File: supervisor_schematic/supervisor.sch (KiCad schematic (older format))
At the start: 25 parts

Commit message: more supervisor schem work
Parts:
- added C?: CP1, symbol Device:CP1
- added D?: LED, symbol Device:LED
- added J?: Conn_02x03_Odd_Even, symbol Connector_Generic:Conn_02x03_Odd_Even
- added Jack: PJ-059A, PJ059A, symbol Noggin:PJ-059A
- added R9: 330, symbol Device:R
- gave numbers to parts that had none: 2
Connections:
- net labels added: IO0, RX, TX
- wire segments 55 -> 68
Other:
- note added: "Enable"
- moved on the sheet: 10K, ANT?, C2, C3, D1, D2, LS?, R1, R2, R3, R4, R5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

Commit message: supervisor almost done
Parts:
- removed C1: 1u, symbol pspice:C
- removed J?: Conn_02x03_Odd_Even, symbol Connector_Generic:Conn_02x03_Odd_Even
- removed U?: OLED-1602A, symbol Noggin:OLED-1602A
- added C1: 1u, symbol Device:CP1
- added IC?: PCF8574DW, SOIC127P1030X265-16N, symbol Noggin:PCF8574DW
- added J1: Conn_01x06_Female, symbol Connector:Conn_01x06_Female
- added U?: OLED-1602A, symbol Noggin:OLED-1602A
- gave numbers to parts that had none: 1
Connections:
- net labels added: RESET
- wire segments 68 -> 80
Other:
- note added: "Button Debouncing"
- note added: "Buzzer"
- note added: "LED Screen\n"
- note added: "Power via a Jack"
- note added: "Programming Header"
- note added: "Will be using a usbC to serial module that will connect via these connectors. \nhttps://www.superhouse.tv/product/espflasher-esp8266-esp32-usb-serial-flasher/"
- note removed: "Enable"
- moved on the sheet: 10K, ANT?, C2, C3, D1, D2, LS1, R1, R2, R3, R4, R5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

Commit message: schem v1 done
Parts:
- added U?: RFM9-LoRa-Radio, symbol Noggin2:RFM9-LoRa-Radio
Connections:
- net +3V3: now also U?.1 (VIN)
- net CLK: now also U?.5 (SCK)
- net CS: now also U?.8 (CS)
- net GND: now also U?.2 (GND)
- net SD0: now also IC?.15 (SDA)
- net SD1: now also IC?.14 (SCL)
- net SD2: now reaches ANT?.17 (SD2)
- net SD2: now also U?.6 (MISO)
- net SD3: now reaches ANT?.18 (SD3)
- net SD3: now also U?.7 (MOSI)
- net IO16: now reaches ANT?.27 (IO16)
- net IO16: now also U?.3 (EN)
- net IO17: now reaches ANT?.28 (IO17)
- net IO18: now reaches ANT?.30 (IO18)
- net IO18: now also U?.9 (RST)
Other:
- note added: "LoRa for wireless communication"
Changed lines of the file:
@@
 	1    0    0    -1
 $EndComp
-Text GLabel 9200 2200 2    50   Input ~ 0
+Text GLabel 9200 2250 2    50   Input ~ 0
 SD1
-Text GLabel 9200 2100 2    50   Input ~ 0
+Text GLabel 9200 2150 2    50   Input ~ 0
 SD0
 $Comp
@@
 Wire Notes Line
 	8550 1000 8550 1650
+$Comp
+L Noggin2:RFM9-LoRa-Radio U?
+U 1 1 621CB351
+P 5700 6700
+F 0 "U?" V 4875 6650 50  0000 C CNN
+F 1 "RFM9-LoRa-Radio" V 4966 6650 50  0000 C CNN
+F 2 "" H 5700 6700 50  0001 C CNN
+F 3 "" H 5700 6700 50  0001 C CNN
+	1    5700 6700
+	0    1    1    0
+$EndComp
+$Comp
+L power:+3.3V #PWR?
+U 1 1 621CE098
+P 5350 6100
+F 0 "#PWR?" H 5350 5950 50  0001 C CNN
+F 1 "+3.3V" H 5365 6273 50  0000 C CNN
+F 2 "" H 5350 6100 50  0001 C CNN
+F 3 "" H 5350 6100 50  0001 C CNN
+	1    5350 6100
+	1    0    0    -1
+$EndComp
+$Comp
+L power:GND #PWR?
+U 1 1 621CEF67
+P 5350 6250
+F 0 "#PWR?" H 5350 6000 50  0001 C CNN
+F 1 "GND" V 5355 6122 50  0000 R CNN
+F 2 "" H 5350 6250 50  0001 C CNN
+F 3 "" H 5350 6250 50  0001 C CNN
+	1    5350 6250
+	0    1    1    0
+$EndComp
+Text GLabel 4250 3200 2    50   Input ~ 0
+IO16
+Text GLabel 5350 6400 0    50   Input ~ 0
+IO16
+Text GLabel 4250 3300 2    50   Input ~ 0
+IO17
+Text GLabel 5300 6550 0    50   Input ~ 0
+IO17
+Text GLabel 5350 6700 0    50   Input ~ 0
+CLK
+Text GLabel 2850 4200 0    50   Input ~ 0
+SD2
+Text GLabel 2850 4300 0    50   Input ~ 0
+SD3
+Text GLabel 5350 6850 0    50   Input ~ 0
+SD2
+Text GLabel 5350 7000 0    50   Input ~ 0
+SD3
+Text GLabel 5350 7150 0    50   Input ~ 0
+CS
+Text GLabel 5350 7300 0    50   Input ~ 0
+IO18
+Text GLabel 4250 3500 2    50   Input ~ 0
+IO18
+Wire Notes Line
+	4850 5650 6350 5650
+Wire Notes Line
+	6350 5650 6350 7600
+Wire Notes Line
+	6350 7600 4850 7600
+Wire Notes Line
+	4850 7600 4850 5650
+Text Notes 5000 5750 0    50   ~ 0
+LoRa for wireless communication
 $EndSCHEMATC

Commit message: going to layout supervisor
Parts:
- removed C?: CP1, symbol Device:CP1
- removed IC?: PCF8574DW, SOIC127P1030X265-16N, symbol Noggin:PCF8574DW
- added CP4: 10u, Capacitor_SMD:C_0805_2012Metric_Pad1.15x1.40mm_HandSolder, symbol Device:CP1
- added CP5: 0.1u, Capacitor_SMD:C_0805_2012Metric_Pad1.15x1.40mm_HandSolder, symbol Device:CP1
- added IC1: PCF8574DW, Connector_PinHeader_2.54mm:PinHeader_1x04_P2.54mm_Vertical, symbol Noggin:PCF8574DW
- added VR1: U1V10F5, Connector_PinHeader_2.54mm:PinHeader_1x03_P2.54mm_Vertical, symbol Noggin2:U1V10F5
- ANT1: renamed from ANT?; footprint ESP32WROOM32D -> Noggin:ESP32WROOM32D
- C1, C2, C3, D1, D2: footprint (none) -> Capacitor_SMD:C_0805_2012Metric_Pad1.15x1.40mm_HandSolder
- D3: renamed from D?; footprint (none) -> Capacitor_SMD:C_0805_2012Metric_Pad1.15x1.40mm_HandSolder
- J1: footprint (none) -> Connector_PinHeader_2.54mm:PinHeader_1x06_P2.54mm_Vertical
- Jack1: renamed from Jack; footprint PJ059A -> Noggin:PJ059A
- LS1: footprint PS1240P02BT -> Noggin:PS1240P02BT
- R1, R2, R3, R4, R5, R7, R8, R9: footprint (none) -> Resistor_SMD:R_0805_2012Metric_Pad1.15x1.40mm_HandSolder
- R6: renamed from 10K; value R6 -> 10K; footprint (none) -> Resistor_SMD:R_0805_2012Metric_Pad1.15x1.40mm_HandSolder
- SW1, SW2, SW3: renamed from SW?; footprint (none) -> Button_Switch_THT:SW_PUSH_6mm
- U1: renamed from U?; footprint (none) -> Package_DIP:DIP-14_W7.62mm
- U2: renamed from U?; footprint (none) -> Noggin:RFM9x
- gave numbers to parts that had none: 1
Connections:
- net +3V3: now also CP4.1, CP5.1, VR1.3 (VIN); no longer U3.~ (VSS)
- net GND: now also CP4.2, CP5.2, IC1.1 (A0), IC1.2 (A1), IC1.3 (A2), IC1.8 (GND), VR1.2 (GND)
- net SDA: now reaches ANT1.33 (IO21)
- net SDA: now also IC1.15 (SDA)
- net SCL: now reaches ANT1.36 (IO22)
- net SCL: now also IC1.14 (SCL)
- new net: IC1.10 (P5), U3.~ (VSS)
- new net: IC1.11 (P6), U3.~ (VSS)
- new net: IC1.4 (P0), U3.~ (VSS)
- new net: IC1.5 (P1), U3.~ (VSS)
- new net: IC1.6 (P2), U3.~ (VSS)
- new net: IC1.7 (P3), U3.~ (VSS)
- new net: IC1.9 (P4), U3.~ (VSS)
- new net +5V: IC1.16 (VCC), U3.~ (VSS), VR1.1 (VOUT)
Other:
- note added: "3V to 5V"
- note added: "LED Screen\nusing module\n"
- note removed: "LED Screen\n"

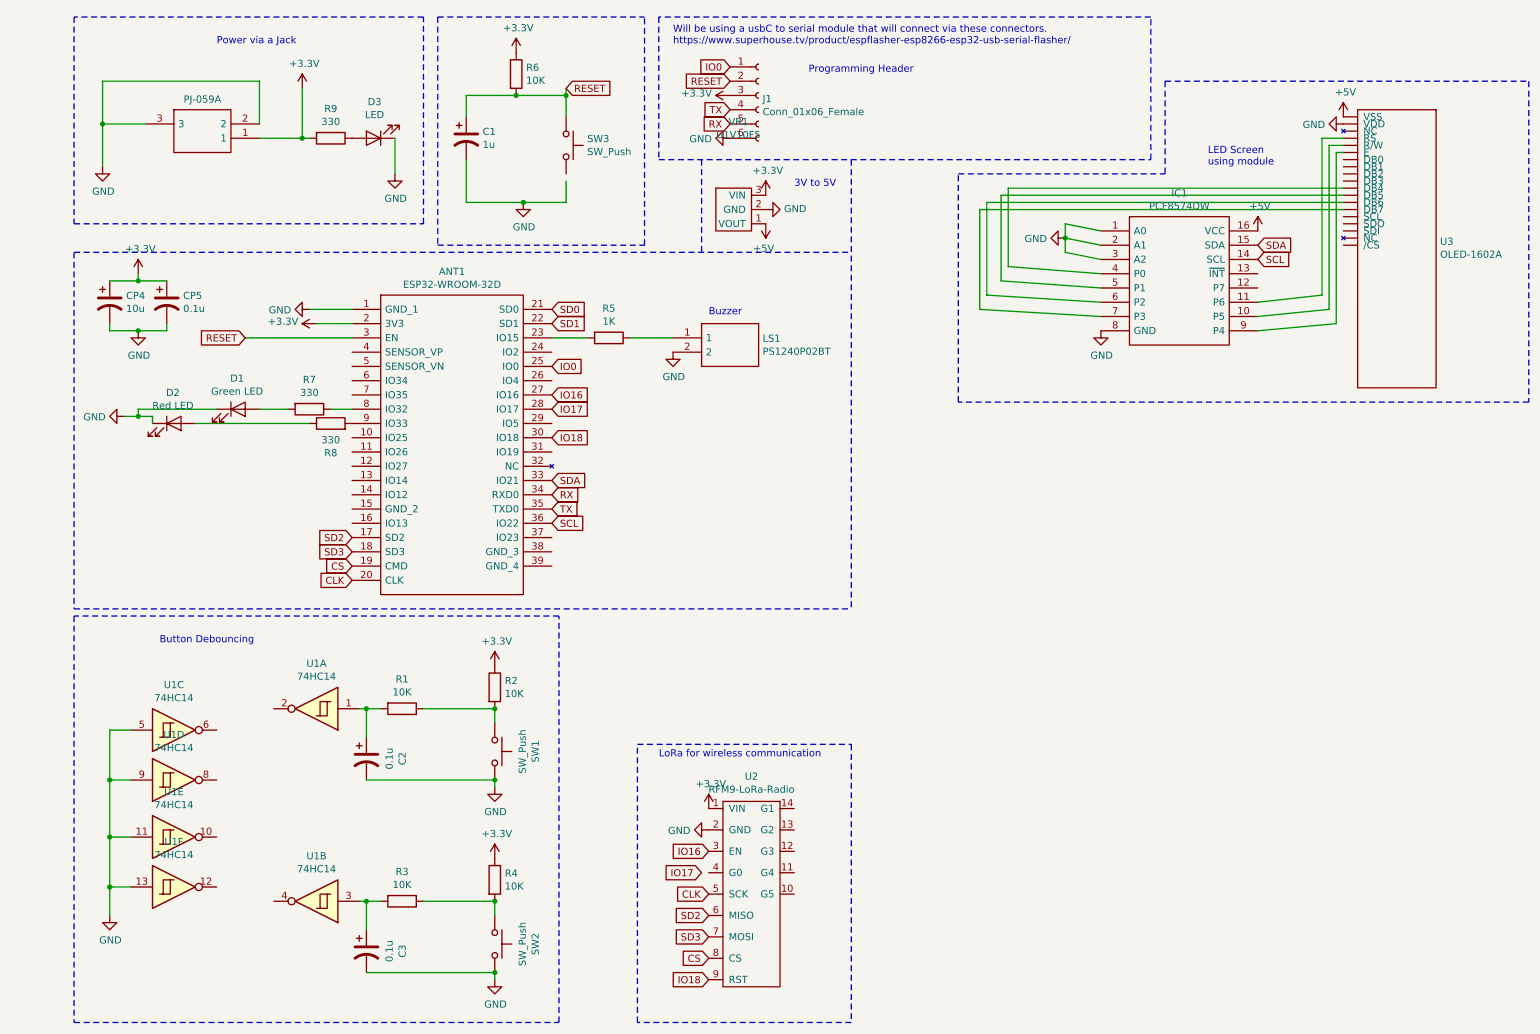
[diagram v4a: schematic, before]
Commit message: ratsnest supervisor
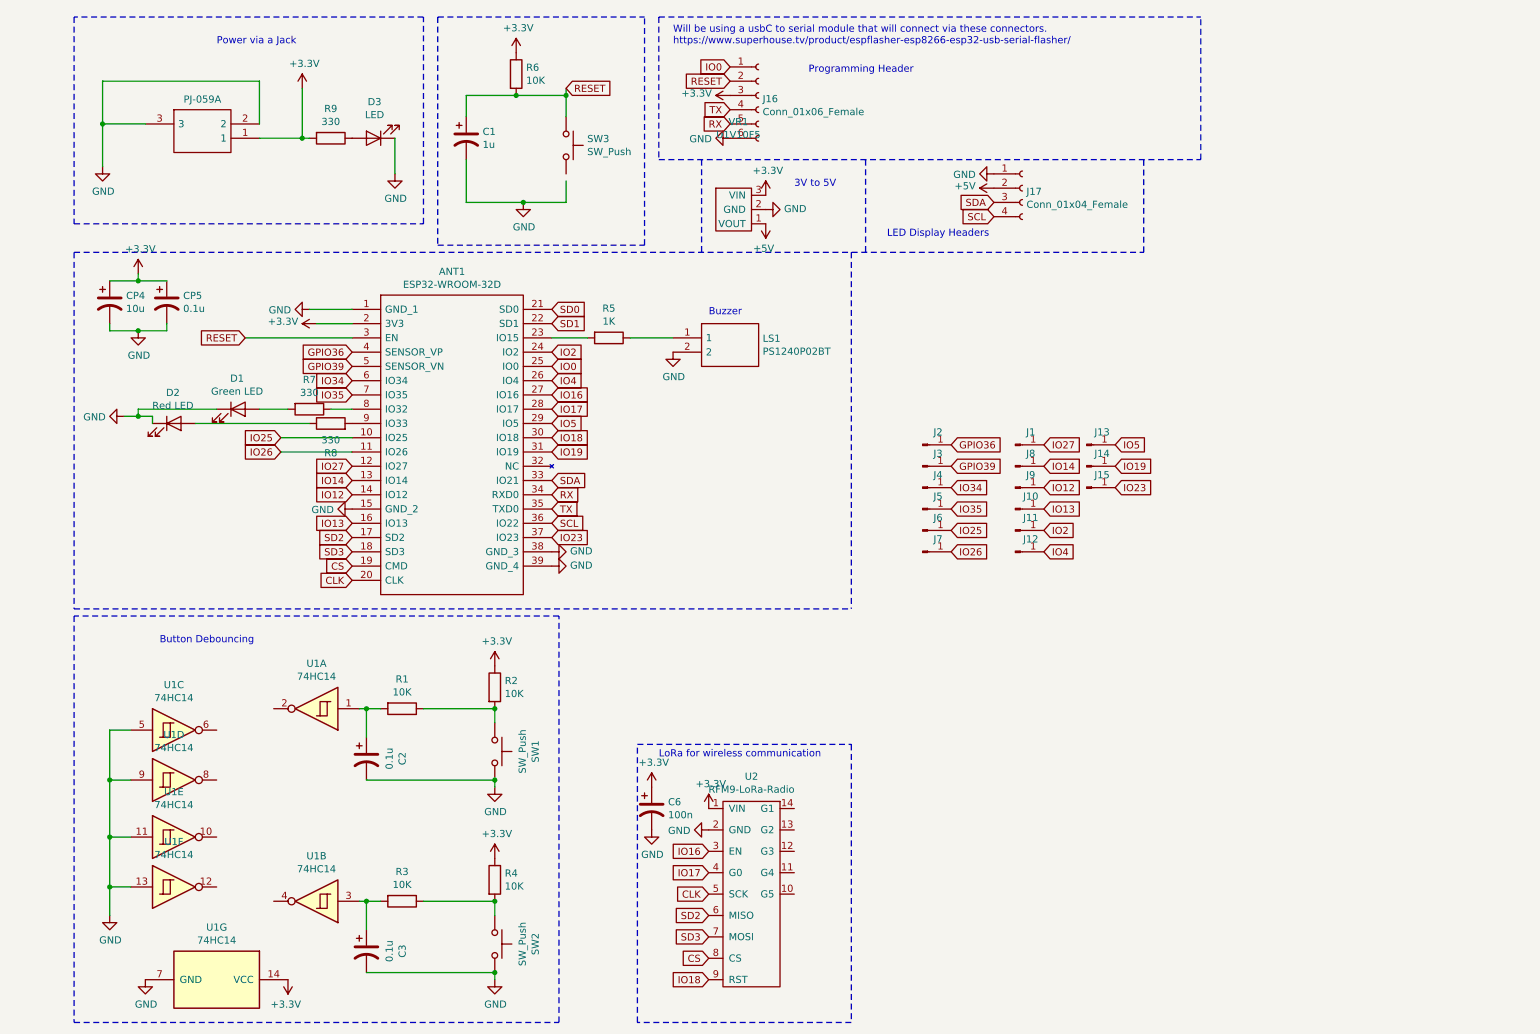
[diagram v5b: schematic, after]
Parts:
- removed IC1: PCF8574DW, Connector_PinHeader_2.54mm:PinHeader_1x04_P2.54mm_Vertical, symbol Noggin:PCF8574DW
- removed U3: OLED-1602A, symbol Noggin:OLED-1602A
- added C6: 100n, Capacitor_SMD:C_0805_2012Metric_Pad1.15x1.40mm_HandSolder, symbol Device:CP1
- added J1, J10, J11, J12, J13, J14, J15, J2, J3, J4, J5, J6, J7, J8, J9: J, Connector_PinHeader_2.54mm:PinHeader_1x01_P2.54mm_Vertical, symbol Connector:Conn_01x01_Male
- added J17: Conn_01x04_Female, symbol Connector:Conn_01x04_Female
- added unit 7 of U1
- VR1: footprint Connector_PinHeader_2.54mm:PinHeader_1x03_P2.54mm_Vertical -> Noggin:U1V10F5-VR
- renumbered J1 to J16
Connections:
- net +3V3: now also C6.1, U1.14 (VCC)
- net +5V: now also J17.2 (Pin_2)
- net GND: now also ANT1.15 (GND_2), ANT1.38 (GND_3), ANT1.39 (GND_4), C6.2, J17.1 (Pin_1), U1.7 (GND)
- net IO17: now also U2.4 (G0)
- net SCL: now also J17.4 (Pin_4)
- net SDA: now also J17.3 (Pin_3)
- net IO25: now reaches ANT1.10 (IO25)
- net IO25: now also J6.1 (Pin_1)
- net IO26: now reaches ANT1.11 (IO26)
- net IO26: now also J7.1 (Pin_1)
- net IO27: now reaches ANT1.12 (IO27)
- net IO27: now also J1.1 (Pin_1)
- net IO14: now reaches ANT1.13 (IO14)
- net IO14: now also J8.1 (Pin_1)
- net IO12: now reaches ANT1.14 (IO12)
- net IO12: now also J9.1 (Pin_1)
- net IO13: now reaches ANT1.16 (IO13)
- net IO13: now also J10.1 (Pin_1)
- net IO2: now reaches ANT1.24 (IO2)
- net IO2: now also J11.1 (Pin_1)
- net IO4: now reaches ANT1.26 (IO4)
- net IO4: now also J12.1 (Pin_1)
- net IO5: now reaches ANT1.29 (IO5)
- net IO5: now also J13.1 (Pin_1)
- net IO19: now reaches ANT1.31 (IO19)
- net IO19: now also J14.1 (Pin_1)
- net IO23: now reaches ANT1.37 (IO23)
- net IO23: now also J15.1 (Pin_1)
- net GPIO36: now reaches ANT1.4 (SENSOR_VP)
- net GPIO36: now also J2.1 (Pin_1)
- net GPIO39: now reaches ANT1.5 (SENSOR_VN)
- net GPIO39: now also J3.1 (Pin_1)
- net IO34: now reaches ANT1.6 (IO34)
- net IO34: now also J4.1 (Pin_1)
- net IO35: now reaches ANT1.7 (IO35)
- net IO35: now also J5.1 (Pin_1)
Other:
- note added: "LED Display Headers\n"
- note removed: "LED Screen\nusing module\n"
